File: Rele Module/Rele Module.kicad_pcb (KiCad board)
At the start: 2 copper layers, 9 parts, among them J1 Screw_Terminal_01x03, J2 Screw_Terminal_01x03, K1 SANYOU_SRD_Form_C, Q1 2N3904

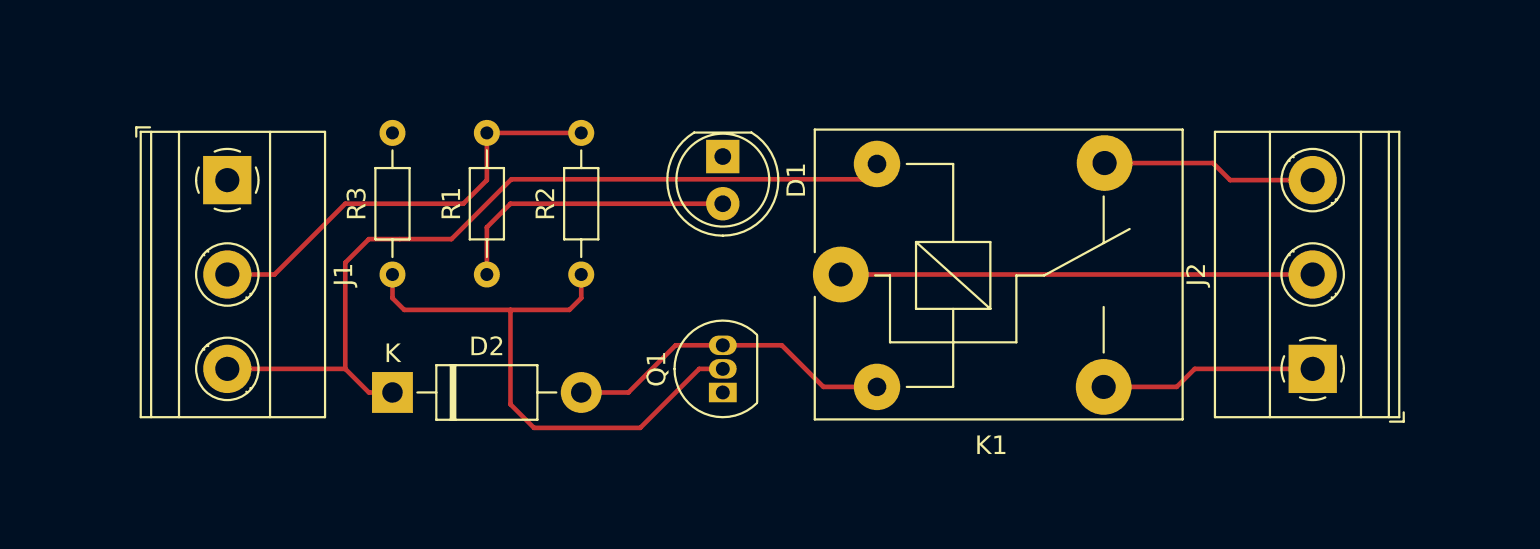
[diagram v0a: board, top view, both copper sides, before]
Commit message: pcb track widening
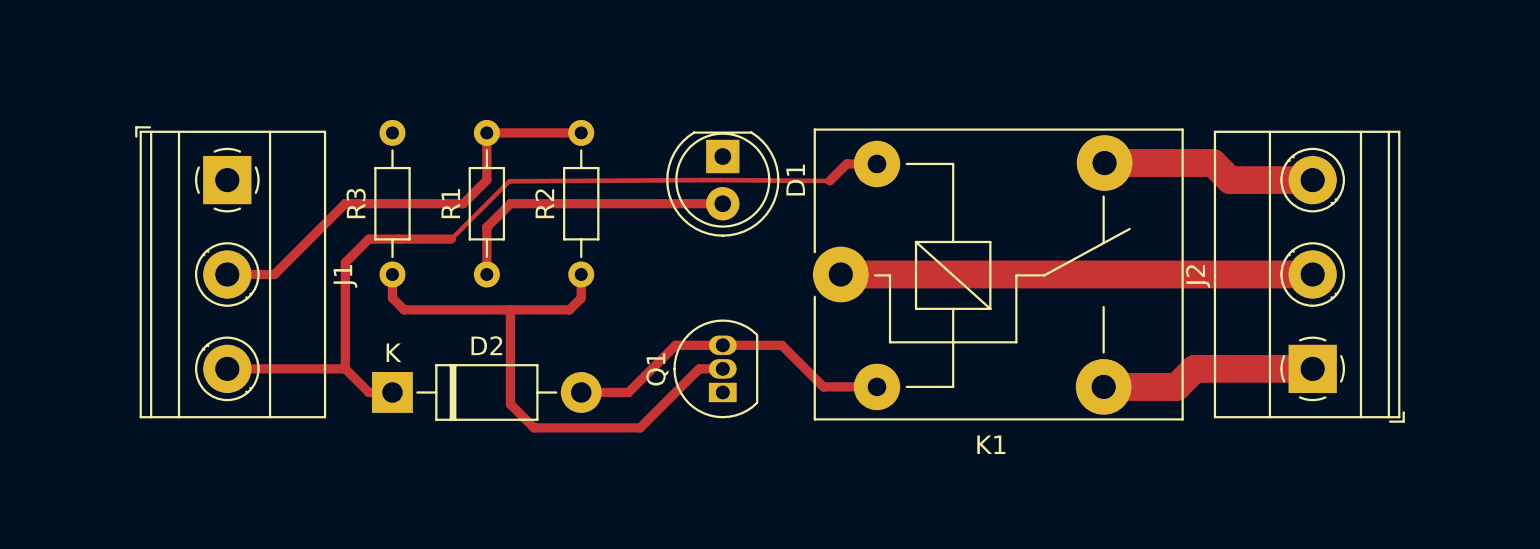
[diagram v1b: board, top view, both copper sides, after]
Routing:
- net VCC: track 46.0 -> 47.1 mm

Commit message: Project completed
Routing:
- added copper zone on B.Cu, net GND
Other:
- board outline added: 78.7 x 25.4 mm

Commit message: Added Images
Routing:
- net VCC: track 47.1 -> 49.8 mm
